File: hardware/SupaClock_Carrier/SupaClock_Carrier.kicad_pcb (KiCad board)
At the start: 2 copper layers, 85 x 67 mm, 25 parts, among them J11 AD8232_SparkFun, J12_LA1 ECG_LA_pad_M3, J12_RA1 ECG_RA_pad_M3, J12_RL1 ECG_RL_pad_M3, J13 AD8232_Pads_RA_LA_RL, J14 MAX30102_bot, J15 XIAO_BAT_Wires, J3 MAX30102_top, J4 MAX30205_8pad, J5 BMI160_7p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

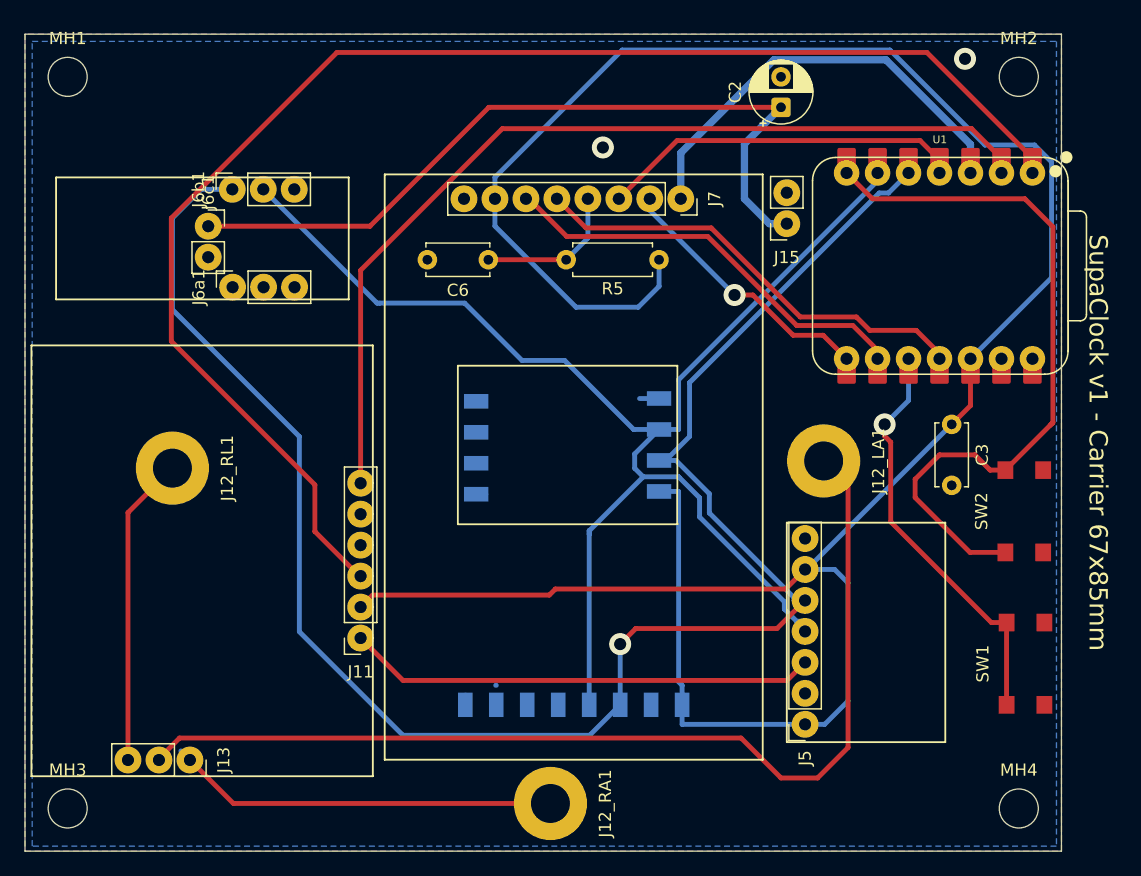
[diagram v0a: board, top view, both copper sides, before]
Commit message: Add UI font and theme management with NVS persistence
- Introduced custom UI fonts in `ui_fonts.h` for better text rendering.
- Created `ui_theme` module with color themes, allowing users to switch themes.
- Implemented NVS storage for persisting the active theme across sessions.
- Added functionality to retrieve and set themes, including a count of available themes.
- Updated `test_general.c` to enhance screen transition animations.
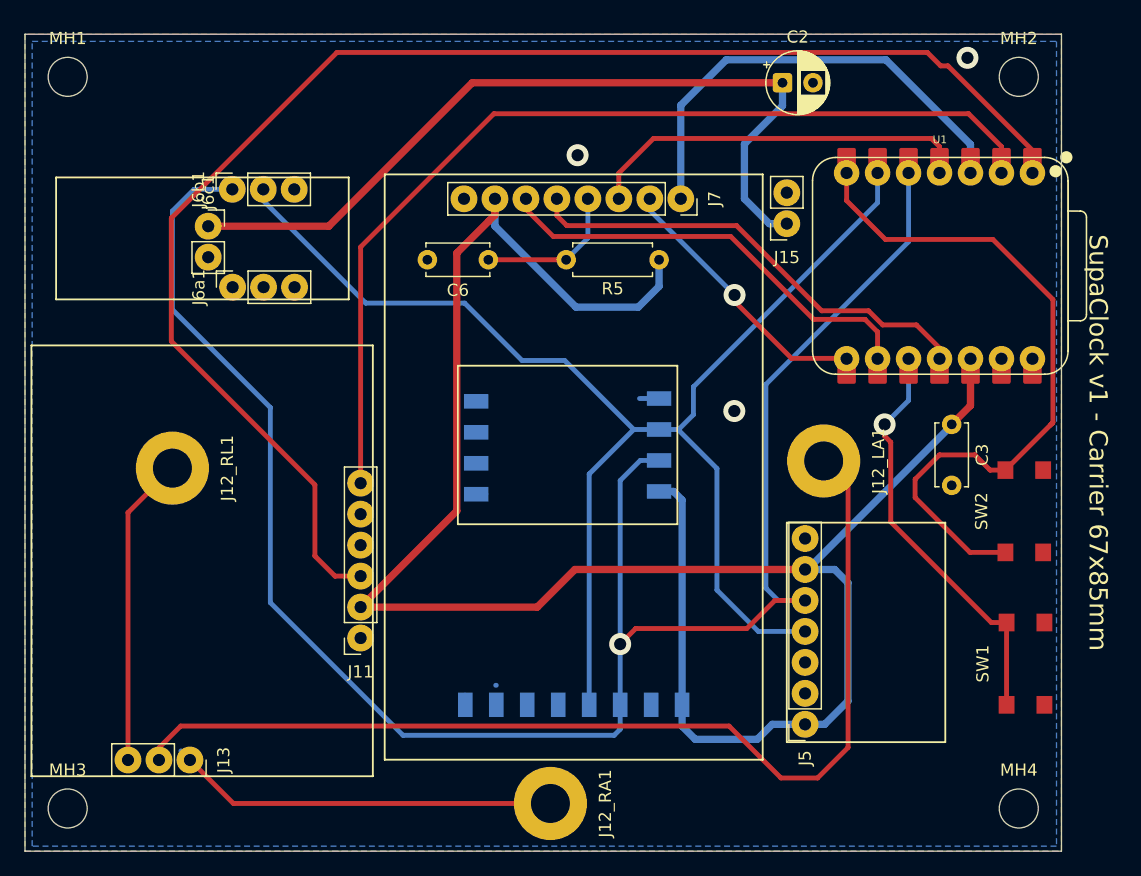
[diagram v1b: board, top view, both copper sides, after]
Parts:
- moved C2 2.02 mm to (126.5, 24.9), turned to 0 degrees
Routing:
- net /GND: track 42.8 -> 4.58 mm, vias 2 -> 3
- net /+3V3: track 206.1 -> 170.6 mm
- net /I2C_SDA: track 149.3 -> 161.6 mm
- net /+BATT: track 64.1 -> 67.1 mm
- net /ECG_SDN: track 77.0 -> 79.7 mm
- net /BLK_PWM: track 36.7 -> 39.0 mm
- net /BTN_NEXT: track 60.9 -> 58.8 mm
- net /SPI_DC: track 30.0 -> 32.0 mm
- net /I2C_SCL: track 117.1 -> 119.0 mm
- net /ECG_OUT: track 116.9 -> 118.4 mm
- net /SPI_SCK: track 34.9 -> 36.3 mm
- net /ECG_LA: track 85.0 -> 86.4 mm
- net /SPI_MOSI: track 37.9 -> 39.0 mm

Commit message: Refactor code structure and remove redundant changes
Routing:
- net /+3V3: track 170.6 -> 174.7 mm
- net /I2C_SCL: track 119.0 -> 121.1 mm
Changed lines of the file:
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@@
 			(drillshape 0)
 			(scaleselection 1)
-			(outputdirectory "gerbersv2/")
+			(outputdirectory "gerbersv3/")
 		)
 	)
@@
 		(tags "M3 electrode ECG screw pad")
 		(property "Reference" "J12_RA1"
-			(at 0 -4.5 90)
+			(at -0.18 -4.5 90)
 			(layer "F.SilkS")
 			(effects
@@
 		)
 		(property "Value" "ECG_RA_pad_M3"
-			(at 0 4.5 90)
+			(at -2.212 6.408 90)
 			(layer "F.Fab")
+			(hide yes)
 			(effects
 				(font
@@
 	)
 	(segment
+		(start 116.84 59.944)
+		(end 118.872 61.976)
+		(width 0.6)
+		(layer "F.Cu")
+		(net "/+3V3")
+	)
+	(segment
+		(start 97.205425 67.894575)
+		(end 105.156 59.944)
+		(width 0.6)
+		(layer "F.Cu")
+		(net "/+3V3")
+	)
+	(segment
 		(start 141.949575 48.364575)
 		(end 141.949575 47.529575)
@@
 	)
 	(segment
+		(start 105.156 59.944)
+		(end 116.84 59.944)
+		(width 0.6)
+		(layer "F.Cu")
+		(net "/+3V3")
+	)
+	(segment
 		(start 99.822 38.862)
 		(end 99.822 60.00715)
@@
 	)
 	(segment
+		(start 122.936 61.976)
+		(end 125.769575 64.809575)
+		(width 0.6)
+		(layer "F.Cu")
+		(net "/+3V3")
+	)
+	(segment
 		(start 141.949575 46.949575)
 		(end 141.949575 47.529575)
@@
 	)
 	(segment
-		(start 102.949575 34.409575)
-		(end 102.949575 35.734425)
+		(start 118.872 61.976)
+		(end 122.936 61.976)
 		(width 0.6)
 		(layer "F.Cu")
@@
 	)
 	(segment
-		(start 109.509575 64.809575)
+		(start 125.769575 64.809575)
 		(end 128.384575 64.809575)
 		(width 0.6)
@@
 	)
 	(segment
-		(start 99.822 60.00715)
-		(end 91.934575 67.894575)
+		(start 102.949575 34.409575)
+		(end 102.949575 35.734425)
 		(width 0.6)
 		(layer "F.Cu")
@@
 	)
 	(segment
-		(start 106.424575 67.894575)
-		(end 109.509575 64.809575)
+		(start 91.934575 67.894575)
+		(end 97.205425 67.894575)
 		(width 0.6)
 		(layer "F.Cu")
@@
 	)
 	(segment
-		(start 91.934575 67.894575)
-		(end 106.424575 67.894575)
+		(start 99.822 60.00715)
+		(end 91.934575 67.894575)
 		(width 0.6)
 		(layer "F.Cu")
@@
 	)
 	(segment
+		(start 114.329575 53.329575)
+		(end 116.409575 53.329575)
+		(width 0.4)
+		(layer "B.Cu")
+		(net "/I2C_SCL")
+	)
+	(segment
 		(start 124.550375 69.889575)
 		(end 121.158 66.4972)
@@
 	)
 	(segment
+		(start 110.679575 56.979575)
+		(end 114.329575 53.329575)
+		(width 0.4)
+		(layer "B.Cu")
+		(net "/I2C_SCL")
+	)
+	(segment
 		(start 110.679575 75.909575)
 		(end 110.679575 56.979575)
@@
 	)
 	(segment
-		(start 128.384575 69.889575)
-		(end 124.550375 69.889575)
+		(start 108.670425 47.670425)
+		(end 110.679575 49.679575)
 		(width 0.4)
 		(layer "B.Cu")
@@
 	)
 	(segment
-		(start 114.329575 53.329575)
-		(end 116.409575 53.329575)
+		(start 128.384575 69.889575)
+		(end 124.550375 69.889575)
 		(width 0.4)
 		(layer "B.Cu")
@@
 	)
 	(segment
-		(start 108.670425 47.670425)
-		(end 114.329575 53.329575)
+		(start 110.679575 49.679575)
+		(end 110.679575 56.979575)
 		(width 0.4)
 		(layer "B.Cu")
@@
 	)
 	(segment
-		(start 110.679575 56.979575)
-		(end 114.329575 53.329575)
-		(width 0.4)
-		(layer "B.Cu")
-		(net "/I2C_SCL")
-	)
-	(segment
 		(start 83.949575 33.634575)
 		(end 83.949575 34.559575)
@@
 	)
 	(segment
-		(start 123.607925 69.652075)
-		(end 125.910425 67.349575)
-		(width 0.4)
-		(layer "F.Cu")
-		(net "/I2C_SDA")
-	)
-	(segment
-		(start 113.219575 70.929575)
-		(end 114.497075 69.652075)
-		(width 0.4)
-		(layer "F.Cu")
-		(net "/I2C_SDA")
-	)
-	(segment
-		(start 114.497075 69.652075)
-		(end 123.607925 69.652075)
+		(start 113.219575 62.992)
+		(end 117.57715 67.349575)
 		(width 0.4)
 		(layer "F.Cu")
@@
 	)
 	(segment
-		(start 125.910425 67.349575)
+		(start 117.57715 67.349575)
 		(end 128.384575 67.349575)
 		(width 0.4)
@@
 	)
 	(via
-		(at 113.219575 70.929575)
+		(at 113.219575 62.992)
 		(size 1.8)
 		(drill 1)
@@
 	(segment
 		(start 113.219575 57.519225)
-		(end 113.219575 70.929575)
+		(end 113.219575 62.992)
 		(width 0.4)
 		(layer "B.Cu")
@@
 		(width 0.4)
 		(layer "B.Cu")
+		(net "/I2C_SDA")
+	)
+	(segment
+		(start 113.219575 62.992)
+		(end 113.219575 70.929575)
+		(width 0.4)
+		(layer "B.Cu")
